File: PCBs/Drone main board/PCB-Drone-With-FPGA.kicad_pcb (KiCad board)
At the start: 4 copper layers, 60 x 100 mm, 207 parts, among them J1001 Conn_02x10, J1002 Conn_02x07, J1003 Conn_02x10, J1004 Conn_02x05, J201 PJ-102A, J601 UJ2-MBH-1-SMT-TR, J801 SMA, J901 Amphenol-1mm-10-header, U1201 10CL040_F484, U301 AP63205WU-7, U401 SC189ZSKTRT, U402 NCP115ASN250T2G, U501 AP63200WU-7, U601 93LCxxBxxOT, U602 FT232H, U603 MT25QL512ABB8ESF-0SIT, U604 W25Q128JVS, U701 ICM-20602, U702 TXB0108PWR, U703 BNO055, U704 DPS422XTSA1, U705 MCP3208, U801 nRF24L01P, U802 RFX2401C, X1401 SiT2001BI-S2-33E-50.000000G, X801 16MHz, Y601 12MHz, Y701 32.7KHz

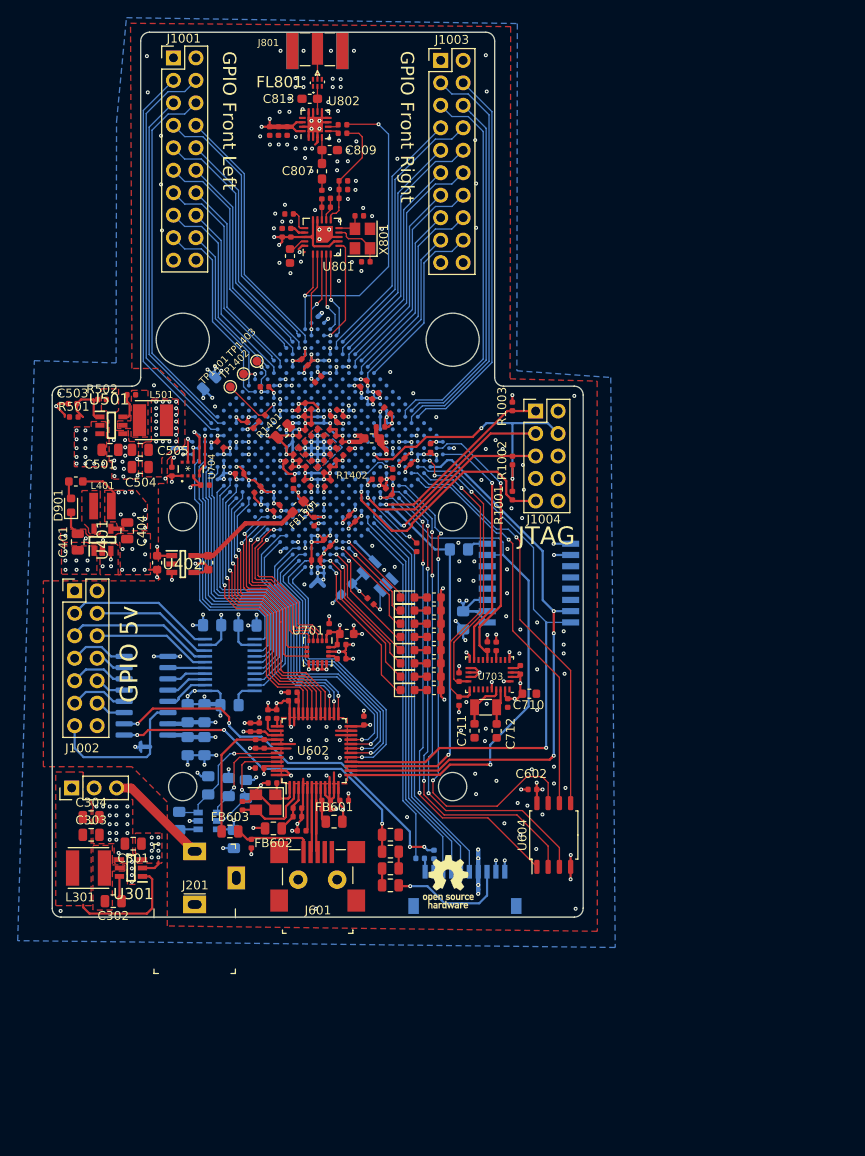
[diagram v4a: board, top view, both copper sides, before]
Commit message: Reworking and checking up to sensors page on main board. Added some datasheets to project
Signed-off-by: Eldalote.Electronics <Eldalote.Electronics@gmail.com>
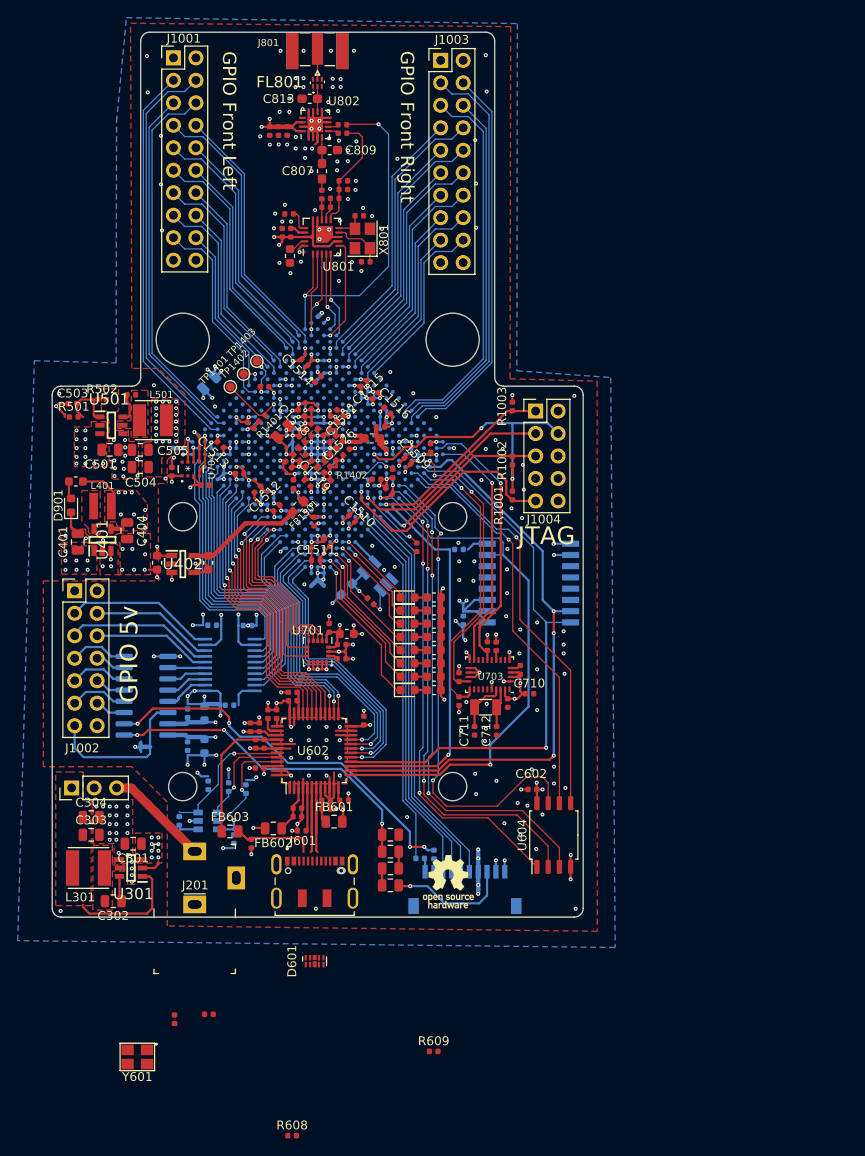
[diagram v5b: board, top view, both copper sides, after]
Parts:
- added D601: ESD7004, Package_DFN_QFN:Diodes_UDFN-10_1.0x2.5mm_P0.5mm, F.Cu at (129.7, 145.0)
- added R608: 5k1, Resistor_SMD:R_0402_1005Metric, F.Cu at (127.1, 164.7)
- added R609: 5k1, Resistor_SMD:R_0402_1005Metric, F.Cu at (143.1, 155.2)
- C1509, C1510, C1511, C1512, C1513, C1514, C1515, C1516, C1519, C1526, C1532, C1538: footprint Inductor_SMD:L_0402_1005Metric -> Capacitor_SMD:C_0402_1005Metric
- C601, C603, C706, C707, C715, C718: footprint Capacitor_SMD:C_0805_2012Metric_Pad1.15x1.40mm_HandSolder -> Capacitor_SMD:C_0402_1005Metric
- C608, C612: value 33pF -> 8.2pF
- C710: footprint Capacitor_SMD:C_0603_1608Metric -> Capacitor_SMD:C_0402_1005Metric
- C711, C712: value 22pF -> 8.2pF; footprint Capacitor_SMD:C_0603_1608Metric -> Capacitor_SMD:C_0402_1005Metric
- C714, C717: footprint Capacitor_SMD:C_0805_2012Metric_Pad1.15x1.40mm_HandSolder -> Capacitor_SMD:C_0603_1608Metric
- J601: value UJ2-MBH-1-SMT-TR -> DX07S016JA1R1500; footprint digikey-footprints:USB_Mini_B_Female_UJ2-MBH-1-SMT-TR -> Eldalote-footprints:JAE_DX07S016JA1R1500
- R601, R602, R603, R604, R605, R704: footprint Resistor_SMD:R_0805_2012Metric_Pad1.15x1.40mm_HandSolder -> Resistor_SMD:R_0402_1005Metric
- Y601: footprint Crystal:Crystal_SMD_3225-4Pin_3.2x2.5mm -> Eldalote-footprints:Crystal NDK 3.2x2.5
- moved Y601 32.2 mm to (109.6, 155.8)
- moved C608 27.1 mm to (117.7, 151.0)
- moved C612 25.3 mm to (113.8, 151.5)
- moved J601 5.75 mm to (129.7, 134.8)
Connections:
- C620 pad 1: Net-(C620-Pad1) -> VBUS
- FB603 pad 2: Net-(C620-Pad1) -> VBUS
- J601 pad 1: Net-(C620-Pad1) -> GND
- J601 pad 2: /USB and Flash Memory/USB-D- -> VBUS
- J601 pad 3: /USB and Flash Memory/USB-D+ -> Net-(J601-Pad3)
- J601 pad 5: GND -> /USB and Flash Memory/USB-D-
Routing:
- net Net-(C612-Pad1): track 9.13 -> 0.00 mm
- net VBUS: track 0.00 -> 9.07 mm
- net Net-(C620-Pad1): track 9.07 -> 0.00 mm
- net GND: track 278.4 -> 271.4 mm, vias 328 -> 327
- net Net-(C608-Pad1): track 4.75 -> 0.42 mm

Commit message: Finished (?) the schematic check and update. Next: PCB update
Signed-off-by: Eldalote.Electronics <Eldalote.Electronics@gmail.com>
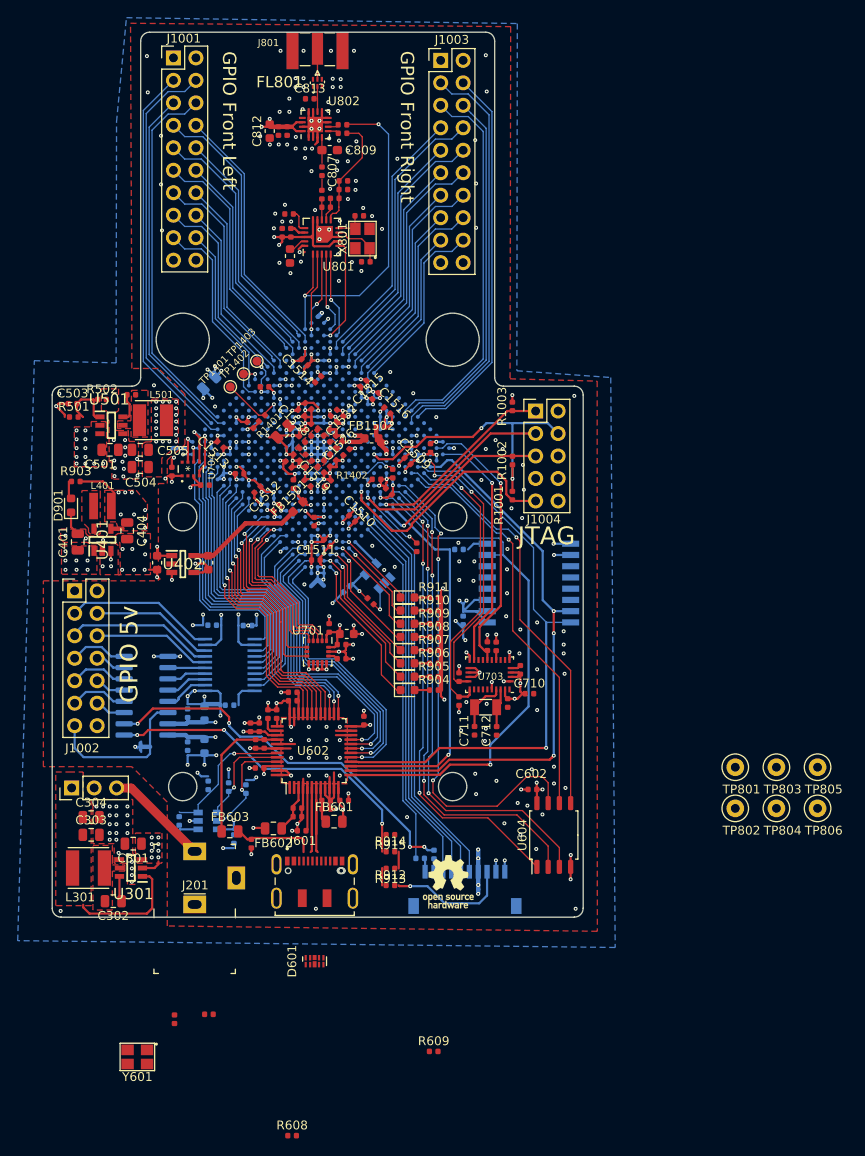
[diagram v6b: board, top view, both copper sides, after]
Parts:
- added TP801: TestPoint, TestPoint:TestPoint_Loop_D2.50mm_Drill1.0mm, F.Cu at (177.2, 123.1)
- added TP802: TestPoint, TestPoint:TestPoint_Loop_D2.50mm_Drill1.0mm, F.Cu at (177.2, 127.7)
- added TP803: TestPoint, TestPoint:TestPoint_Loop_D2.50mm_Drill1.0mm, F.Cu at (181.8, 123.1)
- added TP804: TestPoint, TestPoint:TestPoint_Loop_D2.50mm_Drill1.0mm, F.Cu at (181.8, 127.7)
- added TP805: TestPoint, TestPoint:TestPoint_Loop_D2.50mm_Drill1.0mm, F.Cu at (186.5, 123.1)
- added TP806: TestPoint, TestPoint:TestPoint_Loop_D2.50mm_Drill1.0mm, F.Cu at (186.5, 127.7)
- C1401: footprint Inductor_SMD:L_0603_1608Metric_Pad1.05x0.95mm_HandSolder -> Inductor_SMD:L_0402_1005Metric
- C804, C805: value 15pF -> 8.2pF
- C807, C813: footprint Capacitor_SMD:C_0603_1608Metric_Pad1.05x0.95mm_HandSolder -> Capacitor_SMD:C_0402_1005Metric
- C812: footprint Capacitor_SMD:C_0402_1005Metric -> Capacitor_SMD:C_0603_1608Metric
- FB1501, FB1502: footprint Inductor_SMD:L_0603_1608Metric_Pad1.05x0.95mm_HandSolder -> Inductor_SMD:L_0603_1608Metric
- R903, R904, R905, R906, R907, R908, R909, R910, R911: footprint Resistor_SMD:R_0603_1608Metric -> Resistor_SMD:R_0402_1005Metric
- R912, R913, R914, R915: footprint Resistor_SMD:R_0805_2012Metric -> Resistor_SMD:R_0402_1005Metric
- X1401: footprint Package_TO_SOT_SMD:SOT-23-5_HandSoldering -> Package_TO_SOT_SMD:SOT-23-5
- X801: footprint Crystal:Crystal_SMD_3225-4Pin_3.2x2.5mm -> Eldalote-footprints:Crystal NDK 3.2x2.5
